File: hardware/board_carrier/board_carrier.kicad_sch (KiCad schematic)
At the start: 19 parts, among them J1 Conn_01x08, J2 Conn_01x08, J3 Conn_02x06_Top_Bottom, U1 TJA1051T-3, U2 LM78M05_TO252

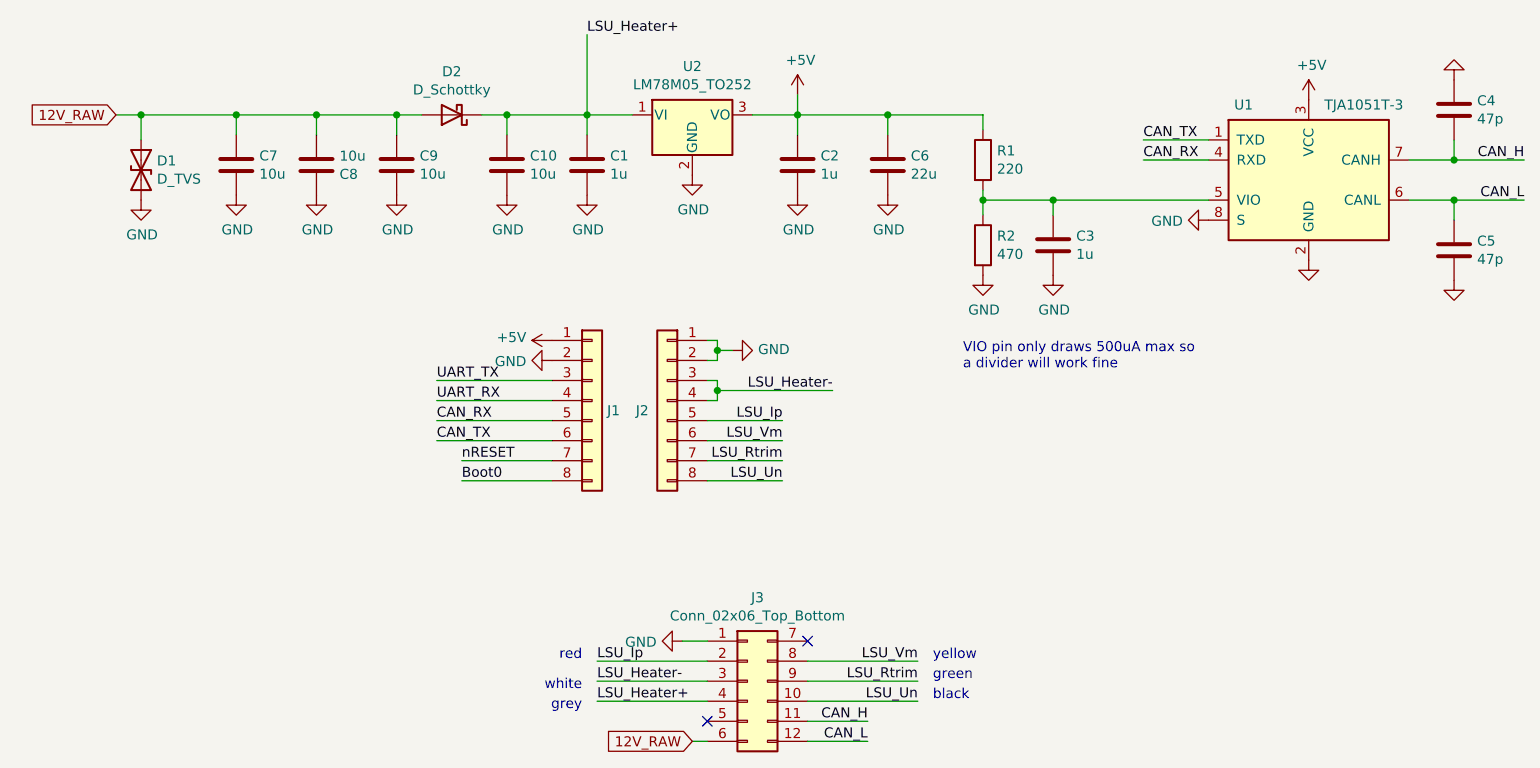
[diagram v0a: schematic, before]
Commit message: reroute carrier for proper footprint
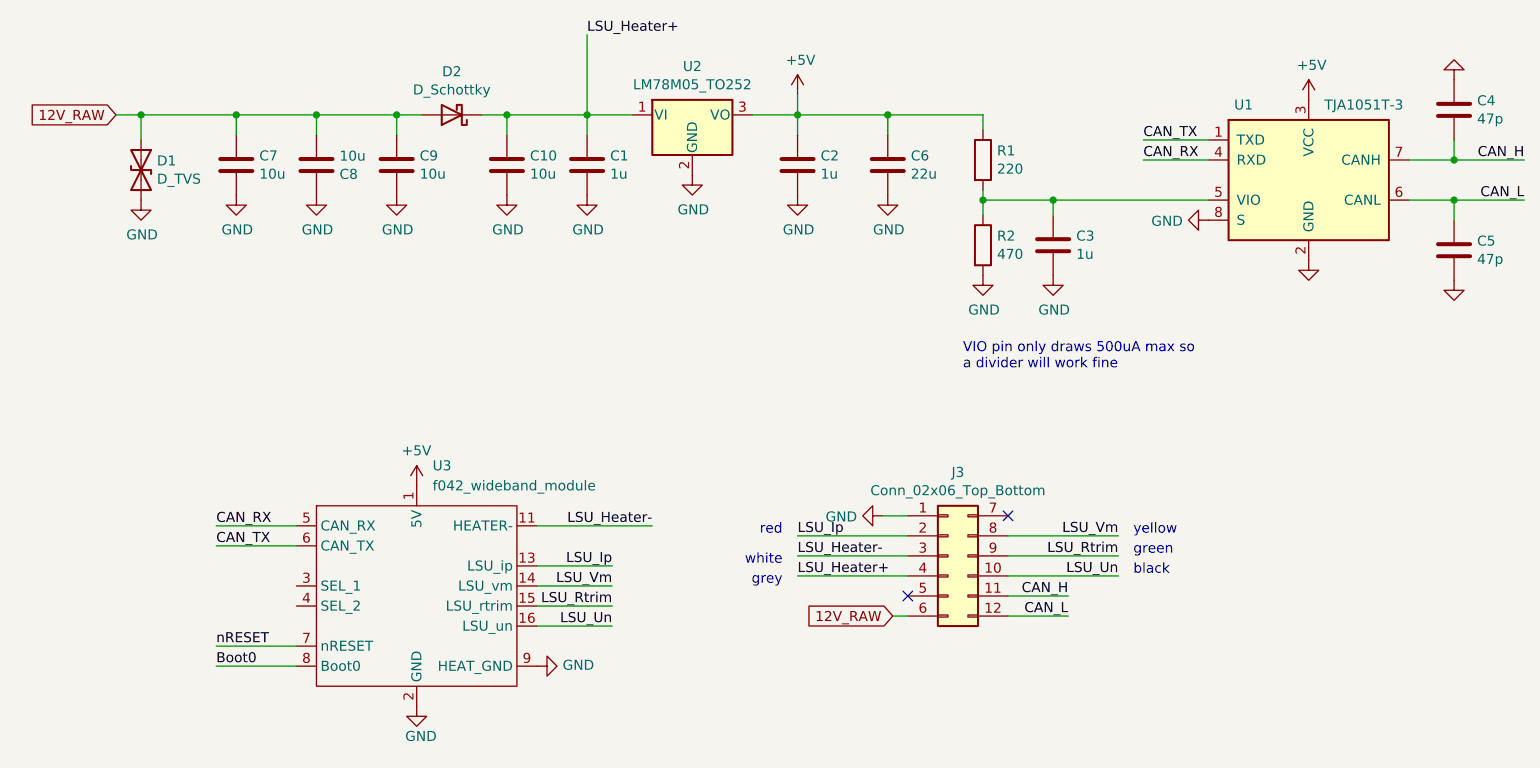
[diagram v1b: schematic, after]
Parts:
- removed J1, J2: Conn_01x08, Connector_PinSocket_2.54mm:PinSocket_1x08_P2.54mm_Vertical, symbol Connector_Generic:Conn_01x08
- added U3: f042_wideband_module, wideband_module:f042_wideband_module, symbol wideband_module:f042_wideband_module
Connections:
- net +5V: now also U3.1 (5V)
- net Boot0: now also U3.8 (Boot0)
- net CAN_RX: now also U3.5 (CAN_RX)
- net CAN_TX: now also U3.6 (CAN_TX)
- net GND: now also U3.10 (HEAT_GND2), U3.2 (GND), U3.9 (HEAT_GND)
- net LSU_Heater-: now also U3.11 (HEATER-), U3.12 (HEATER-)
- net LSU_Ip: now also U3.13 (LSU_ip)
- net LSU_Rtrim: now also U3.15 (LSU_rtrim)
- net LSU_Un: now also U3.16 (LSU_un)
- net LSU_Vm: now also U3.14 (LSU_vm)
- net nRESET: now also U3.7 (nRESET)
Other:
- moved on the sheet: J3

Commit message: vbatt sense
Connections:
- net nRESET is gone; now on net LSU_Heater+: U3.7 (VBatt_Sense)
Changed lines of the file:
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@@
     (stroke (width 0) (type default) (color 0 0 0 0))
   )
-  (wire (pts (xy 47.625 143.51) (xy 57.785 143.51))
+  (wire (pts (xy 45.085 143.51) (xy 57.785 143.51))
     (stroke (width 0) (type default) (color 0 0 0 0))
   )
@@
     (effects (font (size 1.27 1.27)) (justify right bottom))
   )
+  (label "LSU_Heater+" (at 45.085 143.51 0)
+    (effects (font (size 1.27 1.27)) (justify left bottom))
+  )
   (label "CAN_RX" (at 47.625 128.27 0)
     (effects (font (size 1.27 1.27)) (justify left bottom))
@@
   )
   (label "LSU_Heater-" (at 121.285 132.08 0)
-    (effects (font (size 1.27 1.27)) (justify left bottom))
-  )
-  (label "nRESET" (at 47.625 143.51 0)
     (effects (font (size 1.27 1.27)) (justify left bottom))
   )
@@
       (reference "U2") (unit 1) (value "LM78M05_TO252") (footprint "Package_TO_SOT_SMD:TO-252-2")
     )
-    (path "/36c9c185-15fe-4611-92b1-31b237558e28"
+    (path "/a98fc7ba-0401-4572-8a8b-5ae23d966fe4"
       (reference "U3") (unit 1) (value "f042_wideband_module") (footprint "wideband_module:f042_wideband_module")
     )
